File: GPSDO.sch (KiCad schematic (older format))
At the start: 41 parts

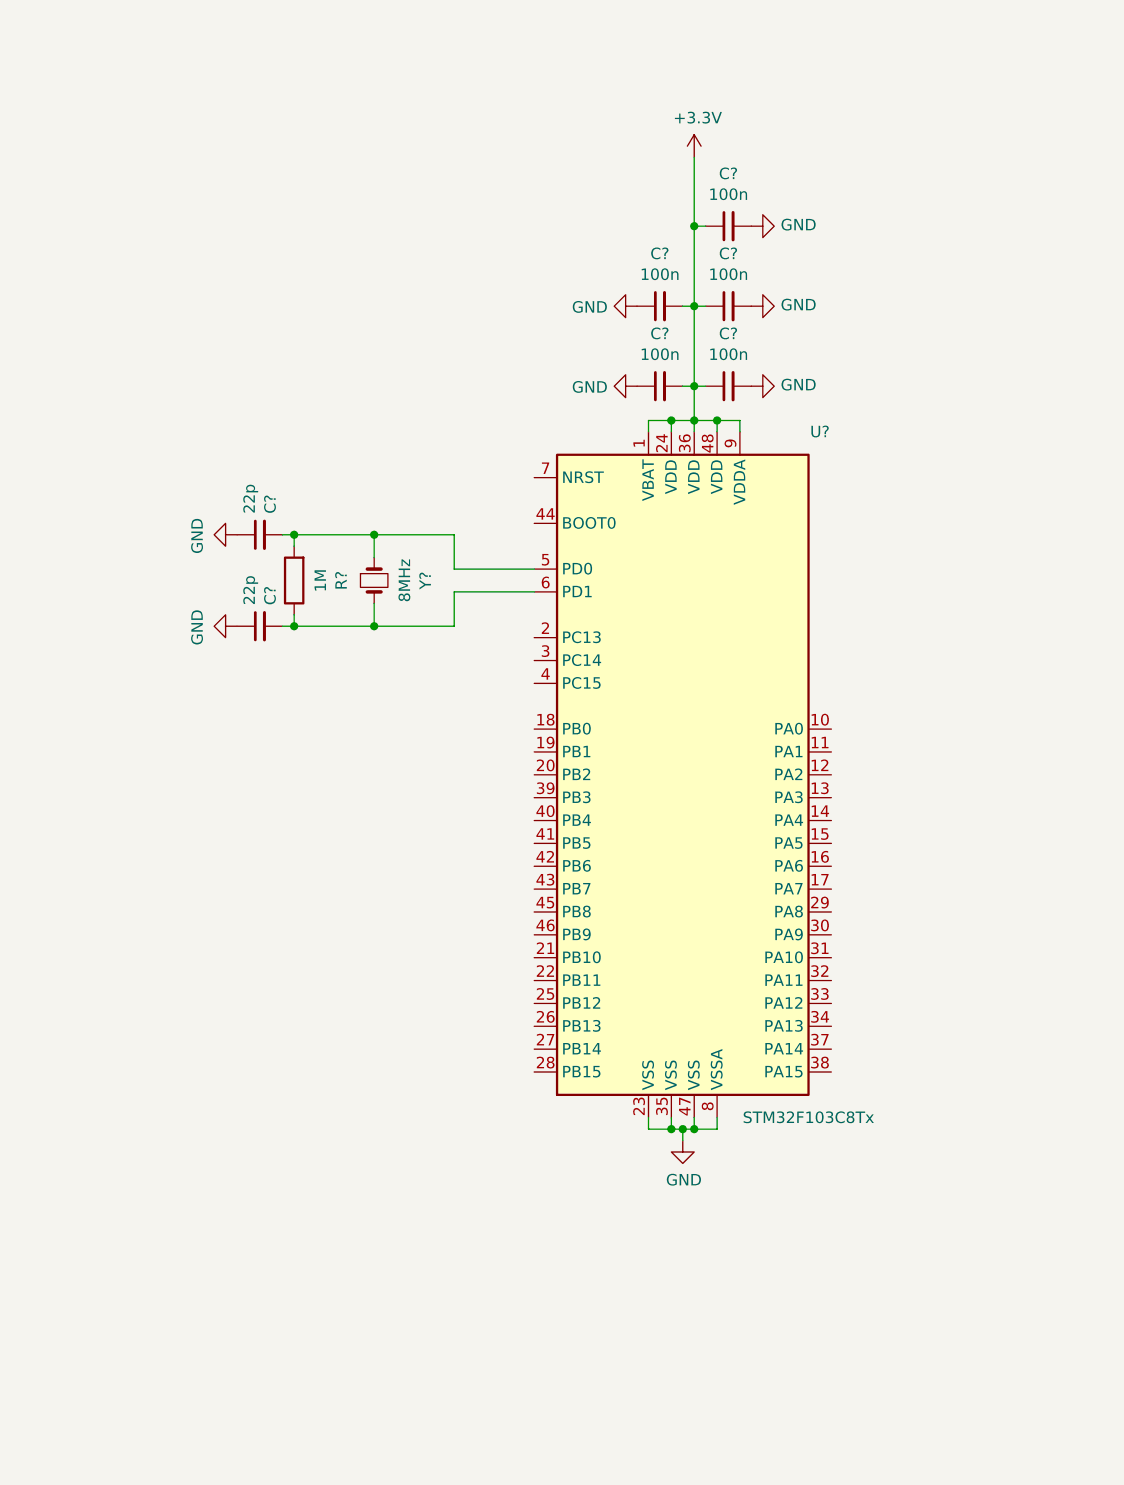
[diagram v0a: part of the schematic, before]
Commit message: Reset, SWD, Boot
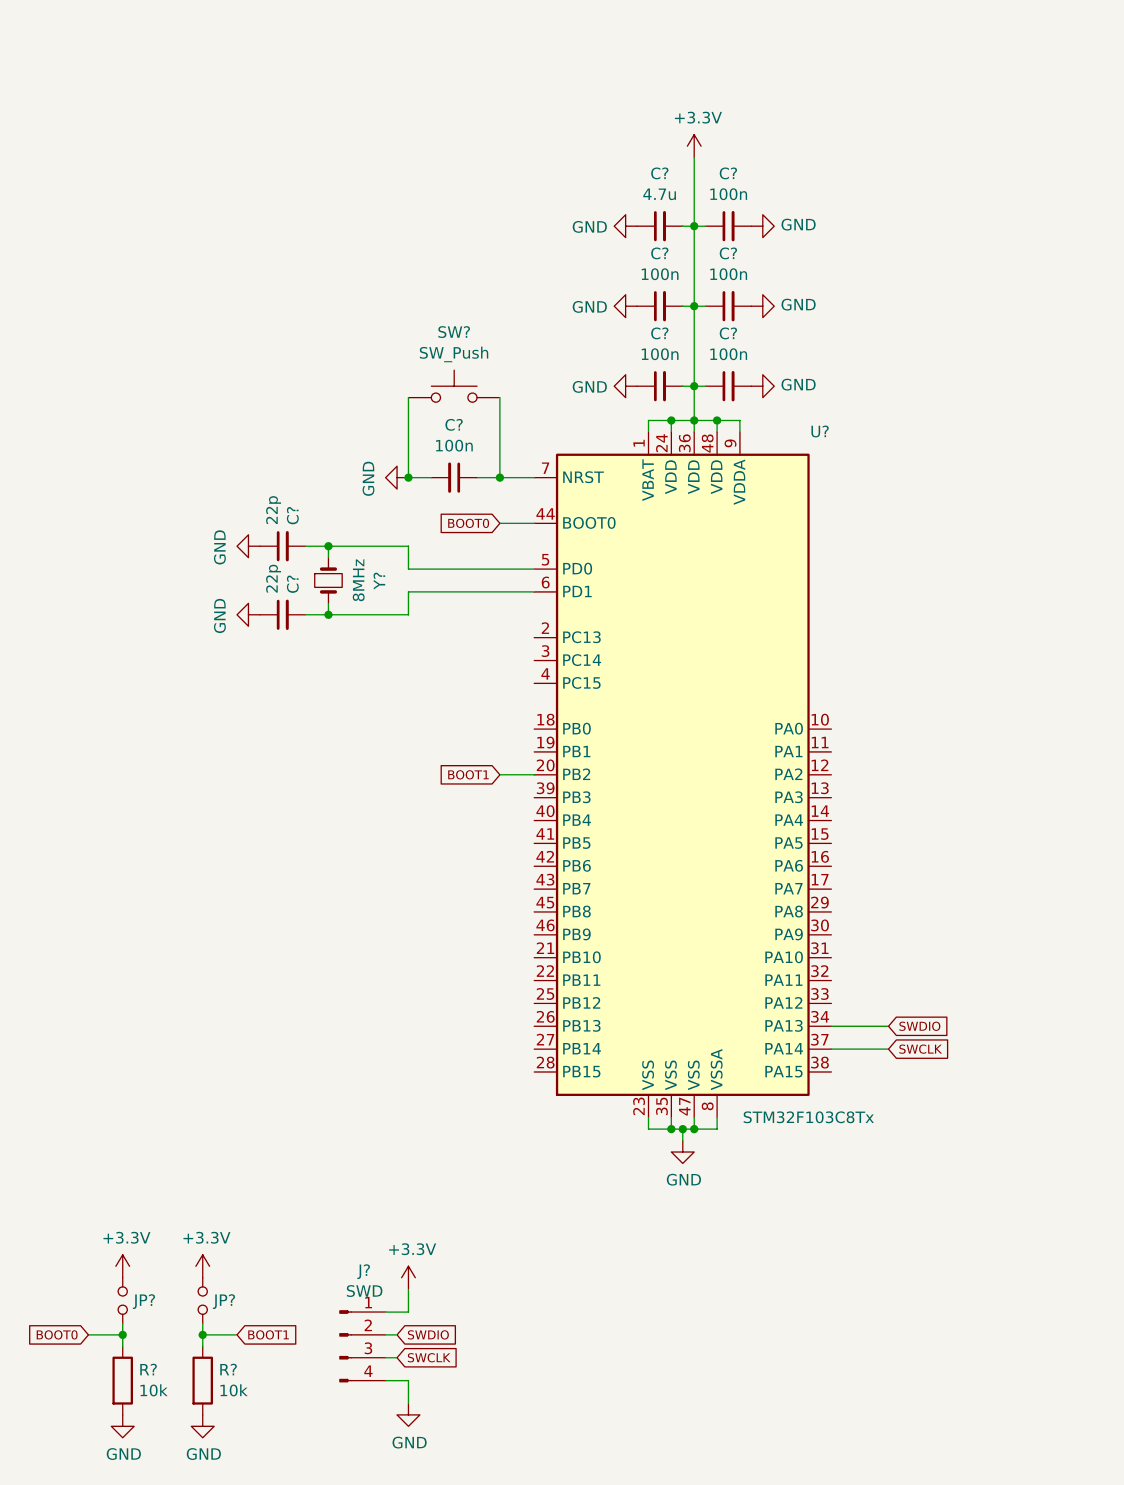
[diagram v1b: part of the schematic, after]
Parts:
- removed R?: 1M, symbol Device:R
- added C?: 100n, symbol Device:C_Small
- added C?: 4.7u, symbol Device:C_Small
- added J?: SWD, symbol Connector:Conn_01x04_Male
- added JP? (x2): Jumper_NO_Small, symbol Device:Jumper_NO_Small
- added R? (x2): 10k, symbol Device:R
- added SW?: SW_Push, symbol Switch:SW_Push
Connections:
- net +3V3: now also C?.2, J?.1 (Pin_1), JP?.1, JP?.1
- net GND: now also C?.1, C?.2, J?.4 (Pin_4), R?.2, R?.2, SW?.1
- net BOOT1: now reaches U?.20 (PB2)
- net BOOT1: now also JP?.2, R?.1
- net SWDIO: now reaches U?.34 (PA13)
- net SWDIO: now also J?.2 (Pin_2)
- net SWCLK: now reaches U?.37 (PA14)
- net SWCLK: now also J?.3 (Pin_3)
- net BOOT0: now reaches U?.44 (BOOT0)
- net BOOT0: now also JP?.2, R?.1
- net at U?.7 (NRST): now also C?.1, SW?.2
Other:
- moved on the sheet: C?, Y?

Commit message: Power Supply
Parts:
- added C?: 470u, symbol Device:CP_Small
- added C? (x3): 100n, symbol Device:C_Small
- added C? (x2): 100u, symbol Device:CP_Small
- added J?: Barrel_Jack, symbol Connector:Barrel_Jack
- added U?: L7805, symbol Regulator_Linear:L7805
- added U?: LM1117-3.3, symbol Regulator_Linear:LM1117-3.3
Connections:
- net +3V3: now also C?.1, C?.1, U?.2 (VO)
- net +5V: now also C?.1, C?.1, U?.3 (OUT), U?.3 (VI)
- net GND: now also C?.2, C?.2, C?.2, C?.2, C?.2, C?.2, J?.2, U?.1 (GND), U?.2 (GND)
- new net: C?.1, C?.1, J?.1, U?.1 (IN)
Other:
- note added: "Power Supply"
- moved on the sheet: BT?, C?, D?, J?, JP?, L?, R?, SW?, U?, U?G, Y?

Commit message: USB
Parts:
- added C? (x2): 22p, symbol Device:C_Small
- added C?: 100n, symbol Device:C_Small
- added J?: USB_B, symbol Connector:USB_B
- added R? (x2): 22R, symbol Device:R
- added R?: 1M, symbol Device:R
- added R?: 1.5k, symbol Device:R
- added U?: NUP2202, Package_TO_SOT_SMD:SOT-363_SC-70-6, symbol Power_Protection:NUP2202
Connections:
- net +5V: now also J?.1 (VBUS), U?.5
- net GND: now also C?.1, C?.2, C?.2, J?.4 (GND), R?.1, U?.2
- new net: J?.2 (D-), R?.1, U?.6
- new net: J?.3 (D+), R?.1, U?.1
- new net: C?.2, J?.5 (Shield), R?.2
- new net USBDM: C?.1, R?.2
- new net USBDP: C?.1, R?.1, R?.2
- new net USBEN: R?.2
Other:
- moved on the sheet: BT?, C?, D?, J?, L?, R?, U?
